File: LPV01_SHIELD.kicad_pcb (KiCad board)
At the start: 4 copper layers, 140 x 125 mm, 106 parts, among them J1 Screw_Terminal_01x02, J10 SPI_header, J11 Power_socket, J12 USB1035-GF-P-0-B-B, J13 USB1035-GF-P-0-B-B, J14 USB1035-GF-P-0-B-B, J15 Screw_Terminal_01x03, J16 Screw_Terminal_01x03, J17 Wiegand, J18 A-USBSA, J19 Screw_Terminal_01x02, J2 Screw_Terminal_01x02, J20 Screw_Terminal_01x02, J21 Screw_Terminal_01x02, J22 Screw_Terminal_01x02, J23 GND, J3 Screw_Terminal_01x02, J4 Screw_Terminal_01x02, J5 Screw_Terminal_01x02, J6 Screw_Terminal_01x02, J7 Screw_Terminal_01x02, J8 Screw_Terminal_01x02, J9 GPIO_header, Q1 BC817, Q2 BC817, Q3 BC817, Q4 BC817, Q5 BC817, Q6 BC817, Q7 BC817, Q8 BC817, SW1 SW_SPST, SW2 SW_SPST, SW3 SW_SPST, SW4 SW_SPST, SW5 SW_SPST, SW6 SW_SPST, SW7 SW_SPST, SW8 SW_SPST, U1 TLP175A, U10 MP2491C, U11 AMS1117-3.3, U12 USB2517I-JZX, U13 FT2232HQ, U14 MIC2026-1xM, U15 MIC2026-1xM, U2 TLP175A, U3 TLP175A, U4 TLP175A, U5 TLP175A, U6 TLP175A, U7 TLP175A, U8 TLP175A, U9 MIC2026-1xM

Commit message: Power schematic update of one DC/DC converter
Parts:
- removed the REF** at (179.4, 57.5)
- added J24: Conn_01x02, Connector_Phoenix_MSTB:PhoenixContact_MSTBA_2,5_2-G_1x02_P5.00mm_Horizontal, F.Cu at (179.6, 57.7)
- added R18: 4k7, Resistor_SMD:R_0603_1608Metric, F.Cu at (136.8, 52.0)
- U9: value MIC2026-1xM -> MP2491C
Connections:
- U10 pad 1: unconnected-(U10-IN-Pad1) -> +24V
- U10 pad 10: unconnected-(U10-MODE-Pad10) -> GND
- U10 pad 11: unconnected-(U10-EN-Pad11) -> Net-(U10-EN)
- U10 pad 12: unconnected-(U10-ILIM-Pad12) -> Net-(U10-ILIM)
- U10 pad 2: unconnected-(U10-PGND-Pad2) -> GND
- U10 pad 3: unconnected-(U10-VCC-Pad3) -> +5V
- U10 pad 4: unconnected-(U10-VSEL1-Pad4) -> +5V
- U10 pad 5: unconnected-(U10-VSEL2-Pad5) -> +5V
- U10 pad 6: unconnected-(U10-FB-Pad6) -> Net-(U10-FB)
- U10 pad 7: unconnected-(U10-AGND-Pad7) -> GND
- U10 pad 8: unconnected-(U10-SW-Pad8) -> Net-(U10-SW)
- U10 pad 9: unconnected-(U10-BST-Pad9) -> Net-(U10-BST)

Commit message: Added values for passive elements near DC/DC
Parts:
- added U16: M24C02-FMN, Package_SO:SOIC-8_3.9x4.9mm_P1.27mm, F.Cu at (3.73, 2.85)
- added U17: MIC2026-1xM, Package_SO:SOIC-8_3.9x4.9mm_P1.27mm, F.Cu at (3.73, 11.4)
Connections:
- U10 pad 10: GND -> Net-(U10-MODE)
- U10 pad 13: unconnected-(U10-PG-Pad13) -> Net-(U10-PG)
- U10 pad 4: +5V -> Net-(U10-VSEL1)
- U10 pad 5: +5V -> Net-(U10-VSEL2)

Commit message: Final version of DC/DC module
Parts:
- removed D10, D12, D14, D16: SMF48CA, Diode_SMD:D_SMA
- removed D11, D13, D15, D9: LED, LED_SMD:LED_0603_1608Metric
- removed J5, J6, J7, J8: Screw_Terminal_01x02, TerminalBlock_Phoenix:TerminalBlock_Phoenix_MKDS-1,5-2_1x02_P5.00mm_Horizontal
- removed Q5, Q6, Q7, Q8: BC817, Package_TO_SOT_SMD:SOT-23
- removed R17, R21, R25, R29: 1k, Resistor_SMD:R_0603_1608Metric
- removed R18 (x2), R19, R22, R23, R26, R27, R30, R31: 4k7, Resistor_SMD:R_0603_1608Metric
- removed R20, R24, R28, R32: 10k, Resistor_SMD:R_0603_1608Metric
- removed SW5, SW6, SW7, SW8: SW_SPST, Button_Switch_SMD:SW_SPST_CK_RS282G05A3
- removed U10: MP2491C, HK:QFN-13_HK
- removed U5, U6, U7, U8: TLP175A, Package_SO:MFSOP6-4_4.4x3.6mm_P1.27mm
- added C1: 100u, Capacitor_THT:CP_Radial_D6.3mm_P2.50mm, F.Cu at (144.8, 51.8)
- added C10: 22u, Capacitor_SMD:C_0805_2012Metric, F.Cu at (117.3, 49.7)
- added C11: 22u, Capacitor_SMD:C_0805_2012Metric, F.Cu at (117.3, 47.7)
- added C12: 22u, Capacitor_SMD:C_0805_2012Metric, F.Cu at (117.4, 64.5)
- added C13: 22u, Capacitor_SMD:C_0805_2012Metric, F.Cu at (117.4, 62.6)
- added C2: 10u, Capacitor_SMD:C_0805_2012Metric, F.Cu at (141.2, 57.5)
- added C3: 10u, Capacitor_SMD:C_0805_2012Metric, F.Cu at (139.3, 57.5)
- added C4: 10u, Capacitor_SMD:C_0805_2012Metric, F.Cu at (137.3, 57.5)
- added C5: 100n, Capacitor_SMD:C_0603_1608Metric, F.Cu at (135.6, 57.5)
- added C6: 1n, Capacitor_SMD:C_0603_1608Metric, F.Cu at (138.0, 63.1)
- added C7: 2u2, Capacitor_SMD:C_0603_1608Metric, F.Cu at (134.1, 54.8)
- added C8: 1u, Capacitor_SMD:C_0603_1608Metric, F.Cu at (126.9, 58.9)
- added C9: 22p, Capacitor_SMD:C_0603_1608Metric, F.Cu at (130.2, 51.5)
- added D1: LED, LED_SMD:LED_0603_1608Metric, F.Cu at (134.5, 64.9)
- added J1: Conn_01x02_Pin, Connector_PinHeader_2.54mm:PinHeader_1x02_P2.54mm_Vertical, F.Cu at (150.2, 64.1)
- added J2: Conn_01x02_Pin, Connector_PinHeader_2.54mm:PinHeader_1x02_P2.54mm_Vertical, F.Cu at (150.2, 48.8)
- added J3: Conn_01x02_Pin, Connector_PinHeader_2.54mm:PinHeader_1x02_P2.54mm_Vertical, F.Cu at (112.1, 61.5)
- added J4: Conn_01x02_Pin, Connector_PinHeader_2.54mm:PinHeader_1x02_P2.54mm_Vertical, F.Cu at (112.1, 51.4)
- added L1: 4u7, HK:Inductor_IHLP3232DZER4R7M11_HK, F.Cu at (119.9, 56.2)
- added R1: 300k, Resistor_SMD:R_0603_1608Metric, F.Cu at (137.9, 61.5)
- added R10: 100k, Resistor_SMD:R_0603_1608Metric, F.Cu at (130.2, 53.1)
- added R11: 1k, Resistor_SMD:R_0603_1608Metric, F.Cu at (138.0, 64.9)
- added R2: 10k, Resistor_SMD:R_0603_1608Metric, F.Cu at (134.0, 51.5)
- added R3: 10k, Resistor_SMD:R_0603_1608Metric, F.Cu at (134.0, 50.1)
- added R4: 51k, Resistor_SMD:R_0603_1608Metric, F.Cu at (132.4, 62.5)
- added R5: 0, Resistor_SMD:R_0603_1608Metric, F.Cu at (129.1, 59.6)
- added R6: 10k, Resistor_SMD:R_0603_1608Metric, F.Cu at (134.5, 62.5)
- added R7: 11k, Resistor_SMD:R_0603_1608Metric, F.Cu at (130.2, 54.5)
- added R8: 0, Resistor_SMD:R_0603_1608Metric, F.Cu at (128.6, 62.6)
- added R9: 0, Resistor_SMD:R_0603_1608Metric, F.Cu at (130.5, 62.6)
- added REF**: Fiducial_0.5mm_Mask1mm, Fiducial:Fiducial_0.5mm_Mask1mm, F.Cu at (108.1, 64.7)
- added REF**: Fiducial_0.5mm_Mask1mm, Fiducial:Fiducial_0.5mm_Mask1mm, F.Cu at (147.1, 47.7)
- added U1: MP2491C, HK:QFN-13_HK, F.Cu at (132.3, 57.8)
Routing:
- net (no net): track 0.00 -> 73.4 mm, vias 0 -> 5
- net Net-(D9-K): track 15.6 -> 0.00 mm, vias 1 -> 0
- net Net-(D15-K): track 15.6 -> 0.00 mm, vias 1 -> 0
- net Net-(D13-K): track 15.6 -> 0.00 mm, vias 1 -> 0
- net Net-(D11-K): track 15.6 -> 0.00 mm, vias 1 -> 0
- net GND: track 14.5 -> 7.25 mm, vias 0 -> 64
- net Net-(D1-K): track 15.6 -> 21.7 mm, vias 1 -> 3
- net Net-(D9-A): track 4.12 -> 0.00 mm, vias 1 -> 0
- net Net-(D15-A): track 4.12 -> 0.00 mm, vias 1 -> 0
- net Net-(D13-A): track 4.12 -> 0.00 mm, vias 1 -> 0
- net Net-(D11-A): track 4.12 -> 0.00 mm, vias 1 -> 0
- net Net-(Q8-B): track 3.36 -> 0.00 mm
- net Net-(Q7-B): track 3.36 -> 0.00 mm
- net Net-(Q6-B): track 3.36 -> 0.00 mm
- net Net-(Q5-B): track 3.36 -> 0.00 mm
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- added copper zone on F.Cu, net (none)
- added copper zone on B.Cu, net +24V
- added copper zone on F.Cu, net +24V
- added copper zone on B.Cu, net +5V
- added copper zone on F.Cu, net +5V
- added copper zone on B.Cu, net GND
- added copper zone on F.Cu, net GND
- added copper zone on In1.Cu, net GND
- added copper zone on In2.Cu, net GND
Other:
- outline, holes or cut-outs redrawn
- board text added: "GND"
- board text added: "IN"
- board text added: "OUT"

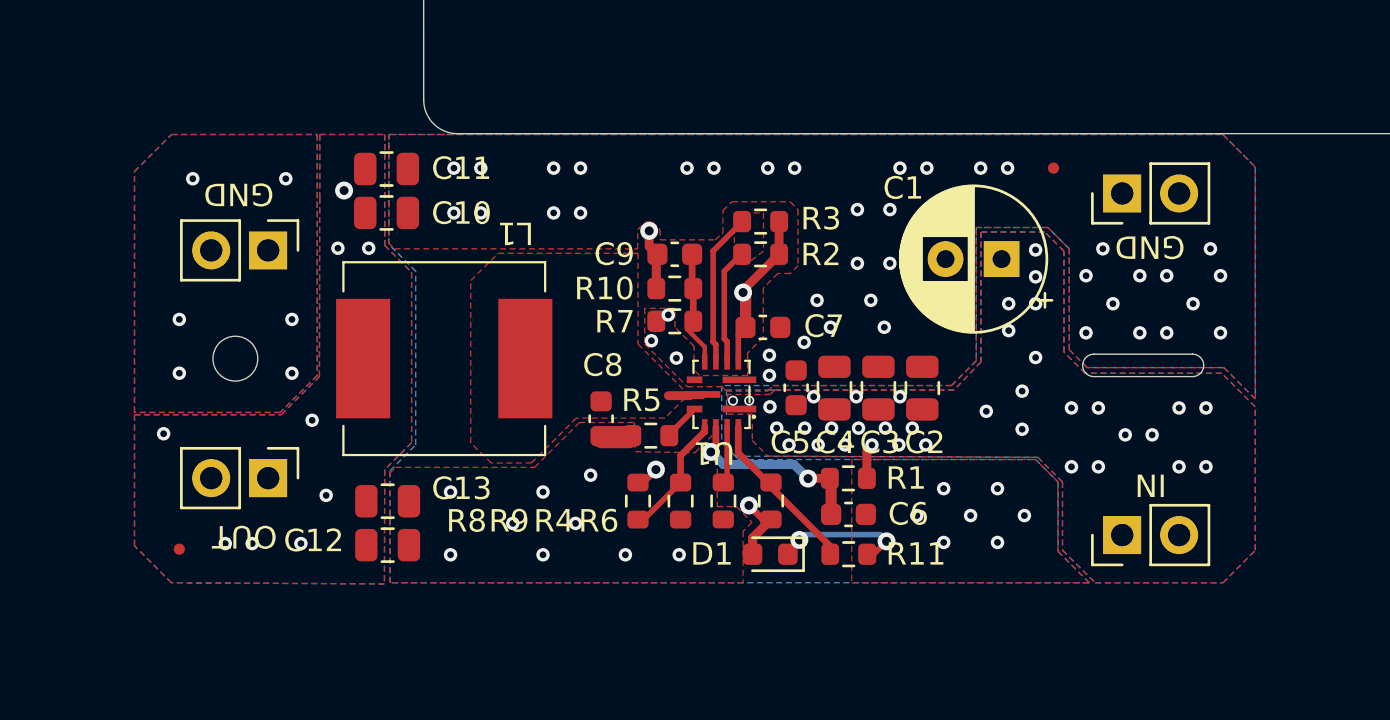
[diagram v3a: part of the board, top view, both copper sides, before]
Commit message: Bigger gaps between +24V and GND
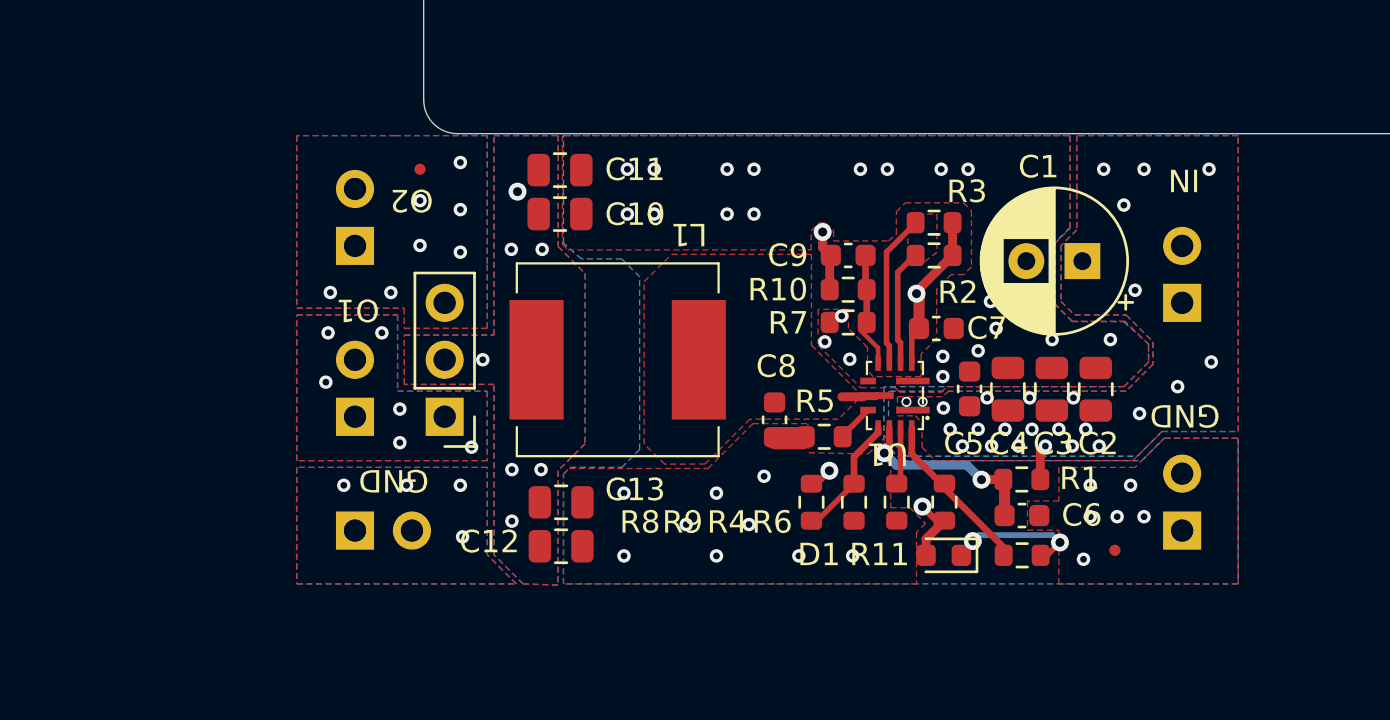
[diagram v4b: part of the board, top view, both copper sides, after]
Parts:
- removed the REF** at (108.1, 64.7)
- removed the REF** at (147.1, 47.7)
- added J5: Conn_01x03_Pin, Connector_PinHeader_2.54mm:PinHeader_1x03_P2.54mm_Vertical, F.Cu at (119.9, 56.2)
- added J6: Conn_01x02_Pin, Connector_PinHeader_2.54mm:PinHeader_1x02_P2.54mm_Vertical, B.Cu at (115.9, 49.9)
- added REF**: Fiducial_0.5mm_Mask1mm, Fiducial:Fiducial_0.5mm_Mask1mm, F.Cu at (118.8, 47.8)
- added REF**: Fiducial_0.5mm_Mask1mm, Fiducial:Fiducial_0.5mm_Mask1mm, F.Cu at (149.8, 64.8)
- J1, J2, J3, J4: moved to B.Cu
- moved J2 14.0 mm to (152.8, 62.6), turned to 0 degrees
- moved J4 13.5 mm to (117.2, 63.9)
- moved J1 11.9 mm to (152.8, 52.4), turned to 0 degrees
- moved R1 7.74 mm to (145.7, 61.6)
- moved R10 7.74 mm to (137.9, 53.1)
- moved R7 7.74 mm to (137.9, 54.6)
- moved R6 7.74 mm to (142.2, 62.6)
- moved R2 7.74 mm to (141.8, 51.6)
- moved C13 7.74 mm to (125.1, 62.6)
- moved C3 7.74 mm to (147.0, 57.6)
- moved C6 7.74 mm to (145.7, 63.2)
- moved C7 7.74 mm to (141.9, 54.9)
- moved R5 7.74 mm to (136.9, 59.7)
- moved R8 7.74 mm to (136.3, 62.6)
- moved U1 7.74 mm to (140.0, 57.8)
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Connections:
- J3 pad 1: +5V -> (no net)
- J3 pad 2: +5V -> (no net)
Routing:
- net (no net): track 73.4 -> 58.0 mm, vias 5 -> 18
- net +5V: track 35.1 -> 20.8 mm, vias 10 -> 8
- net +24V: vias 37 -> 26
- net GND: vias 64 -> 42
- added copper zone on B.Cu, net (none)
- removed copper zone on In1.Cu, net GND
- removed copper zone on In2.Cu, net GND
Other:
- outline, holes or cut-outs redrawn
- board text added: "O1"
- board text added: "O2"
- board text removed: "OUT"
